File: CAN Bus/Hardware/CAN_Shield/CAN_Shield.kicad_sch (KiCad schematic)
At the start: 14 parts, among them J1 Power, J2 PWM, J3 Analog, J4 PWM, J5 Analog, J6 Communication, J7 Digital, J8 Screw_Terminal_01x02, SW2 SW_DIP_x06, U1 MAX3051

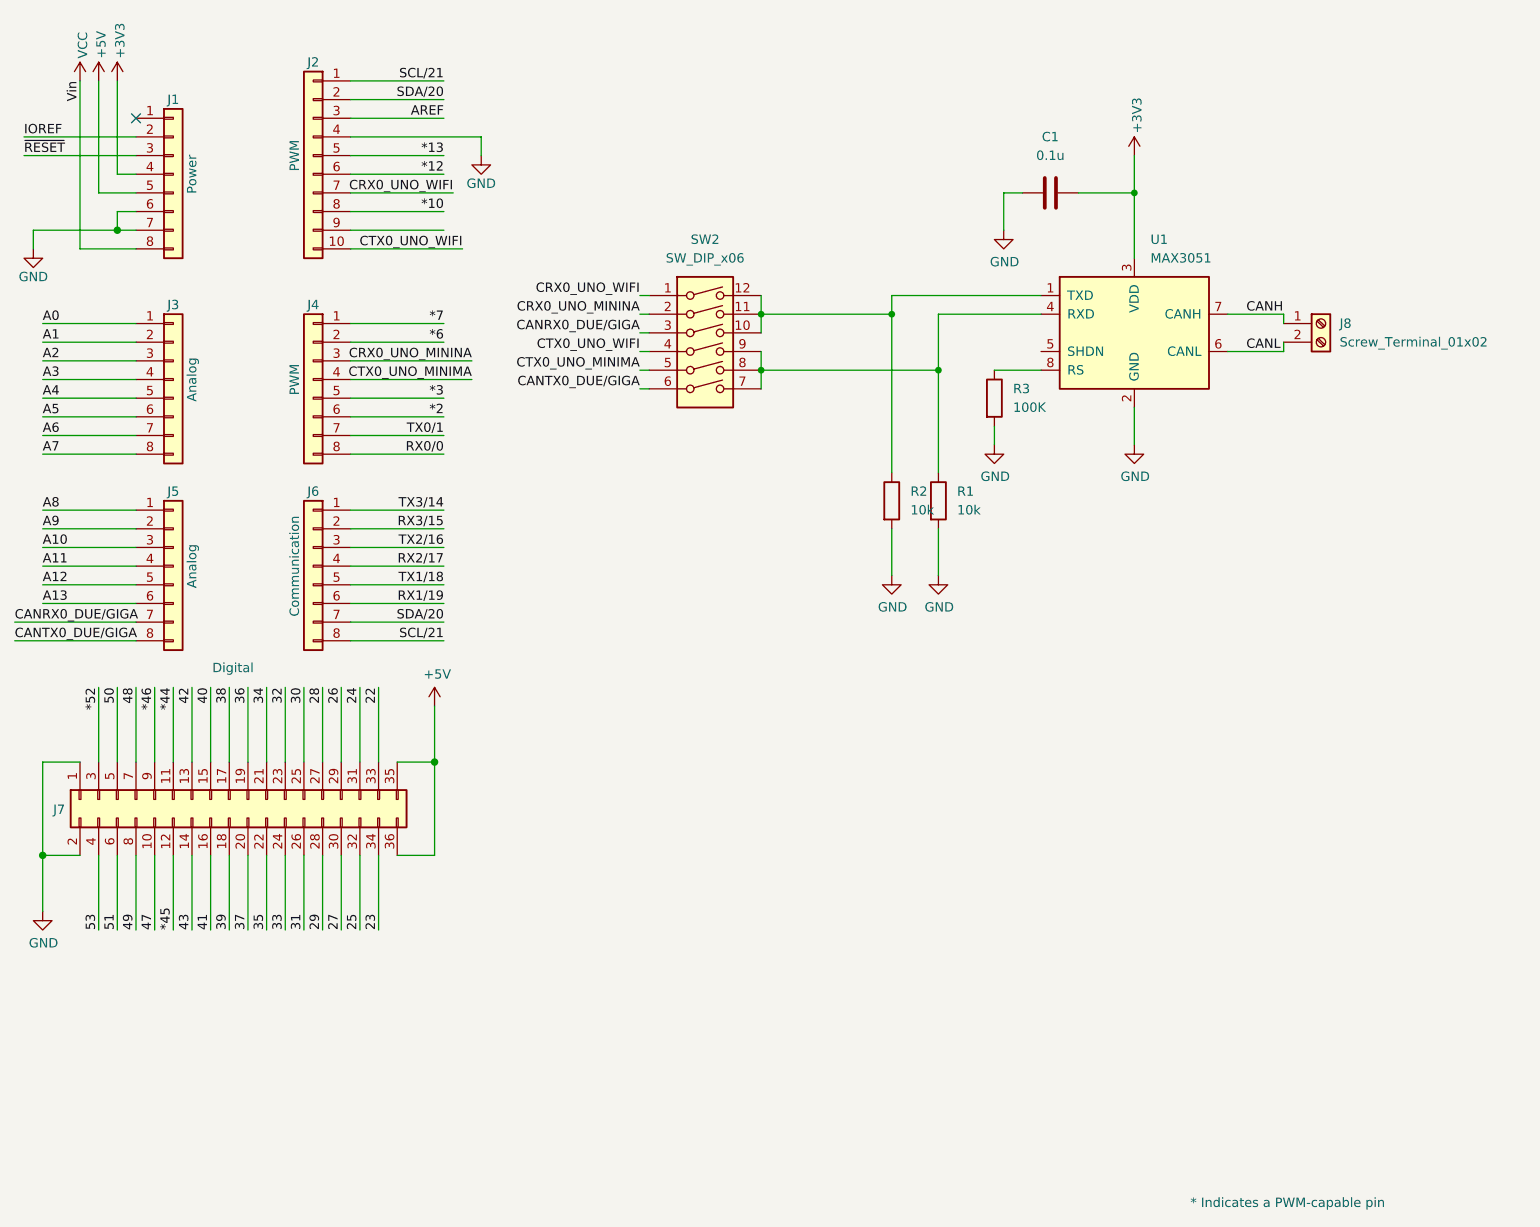
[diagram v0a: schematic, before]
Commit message: fix: change transeiver to TCAN1051HGV-Q1, divide into 2 shield
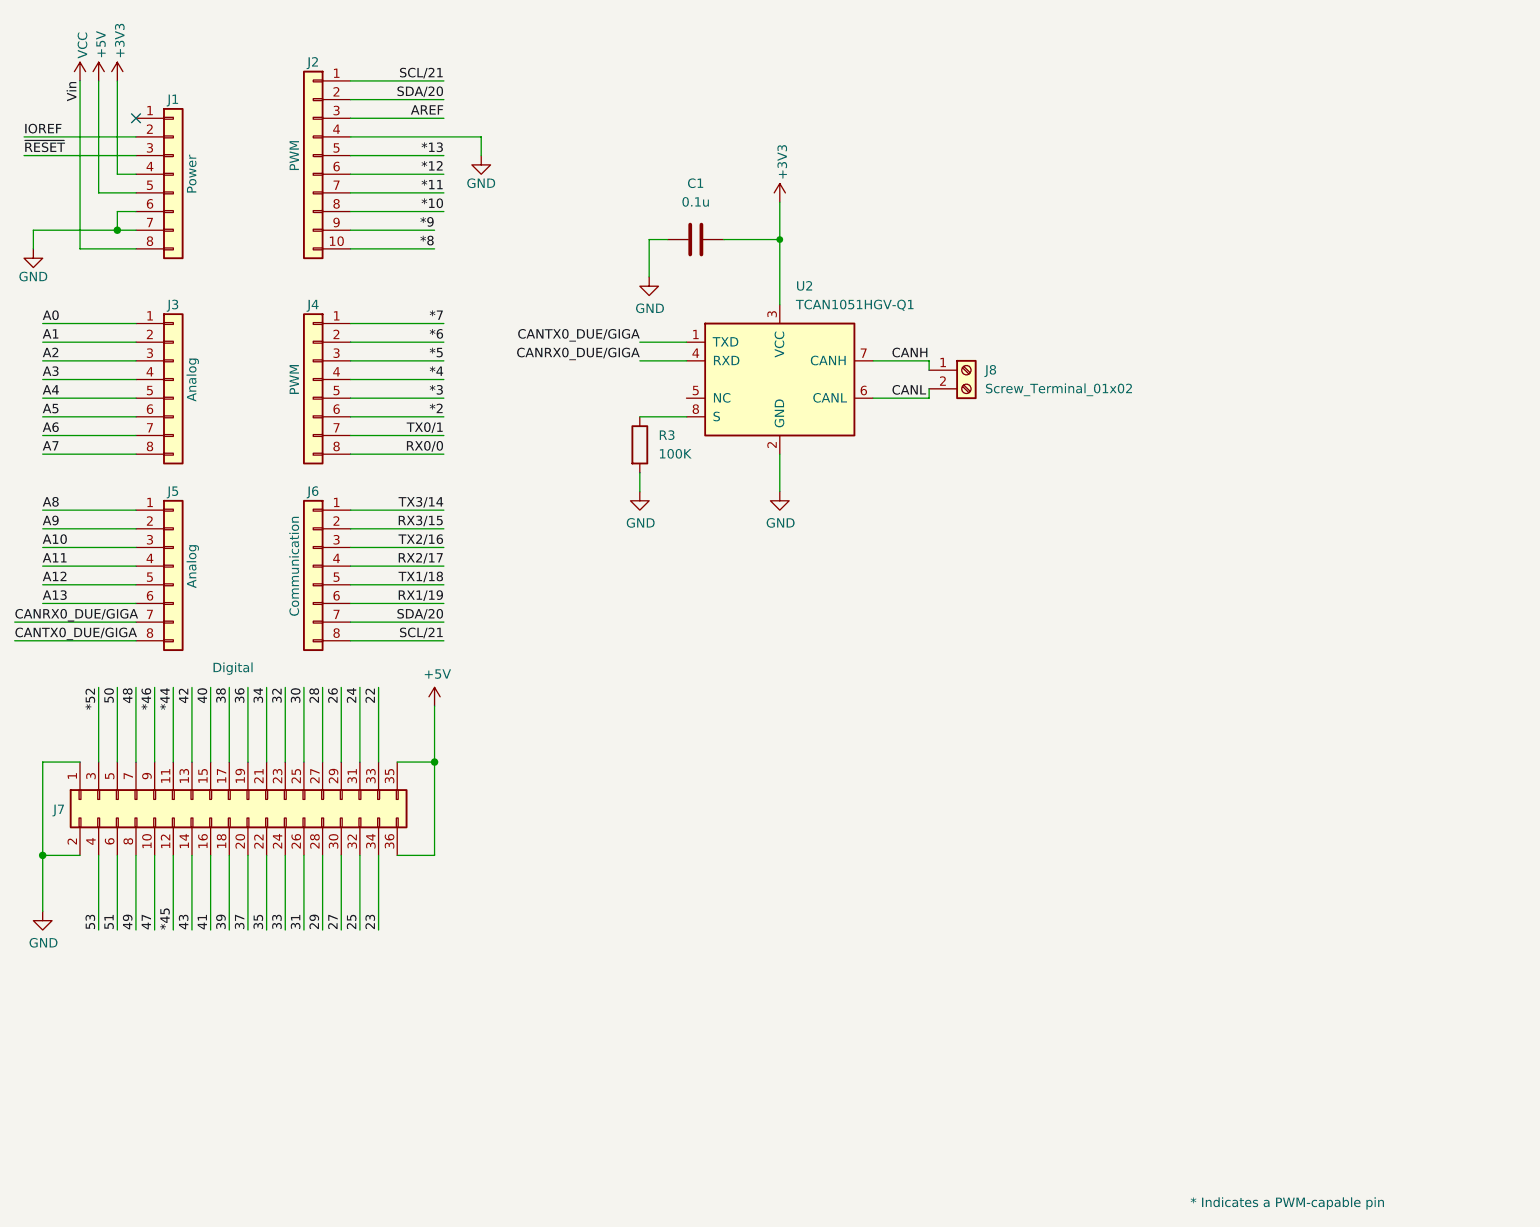
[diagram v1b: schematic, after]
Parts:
- removed R1, R2: 10k, symbol Device:R
- removed SW2: SW_DIP_x06, symbol Switch:SW_DIP_x06
- removed U1: MAX3051, symbol Interface_UART:MAX3051
- added U2: TCAN1051HGV-Q1, symbol CAN_Shield:TCAN1051HGV-Q1
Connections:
- net +3V3: now also U2.3 (VCC)
- net CANH: now also U2.7 (CANH)
- net CANL: now also U2.6 (CANL)
- net CANRX0_DUE/GIGA: now also U2.4 (RXD)
- net CANTX0_DUE/GIGA: now also U2.1 (TXD)
- net GND: now also U2.2 (GND)
- net *9: now reaches J2.9 (Pin_9)
- net at R3.1: now also U2.8 (S)
- net CRX0_UNO_MININA renamed *5
- net CRX0_UNO_WIFI renamed *11
- net CTX0_UNO_MINIMA renamed *4
- net CTX0_UNO_WIFI renamed *8
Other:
- moved on the sheet: C1, J8, R3

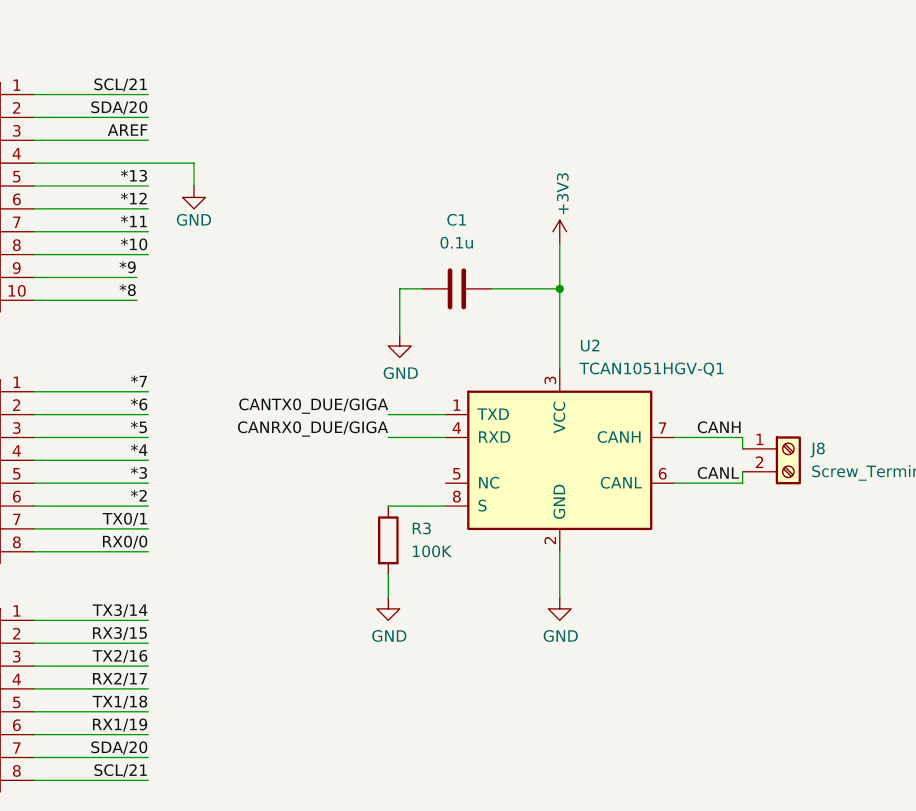
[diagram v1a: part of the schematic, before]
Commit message: fix: change the transeiver, change supply voltages
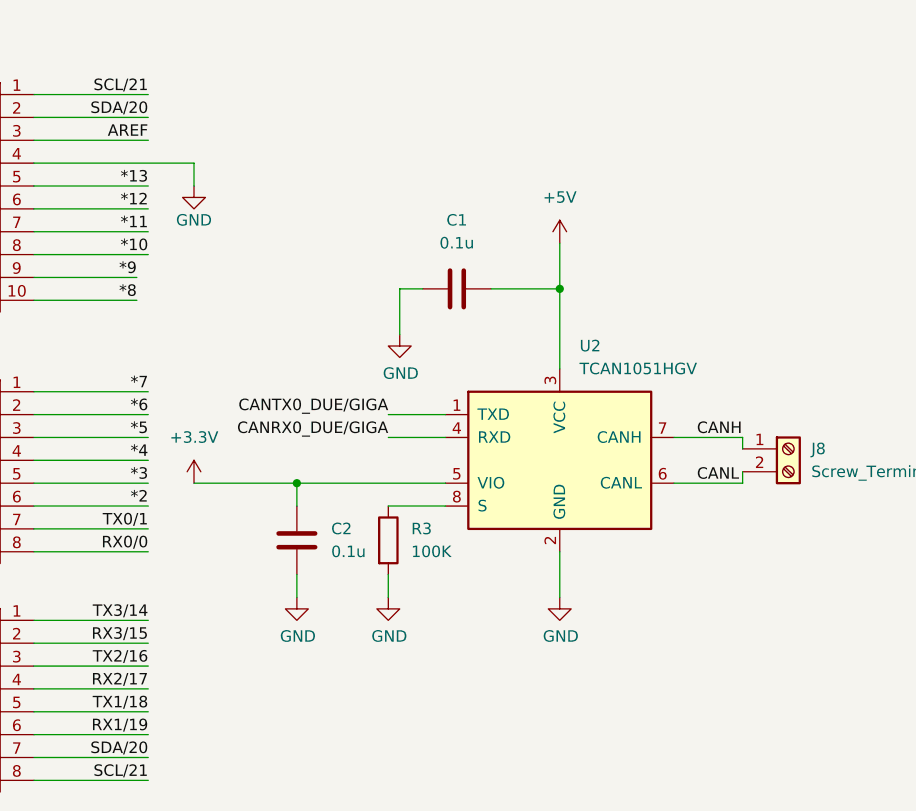
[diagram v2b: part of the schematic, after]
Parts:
- added C2: 0.1u, symbol Device:C
- U2: value TCAN1051HGV-Q1 -> TCAN1051HGV
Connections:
- net +3V3: no longer C1.2, U2.3 (VCC)
- net +5V: now also C1.2, U2.3 (VCC)
- net GND: now also C2.2
- net +3.3V: now reaches U2.5 (VIO)
- net +3.3V: now also C2.1
